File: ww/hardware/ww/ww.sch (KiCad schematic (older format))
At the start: 20 parts

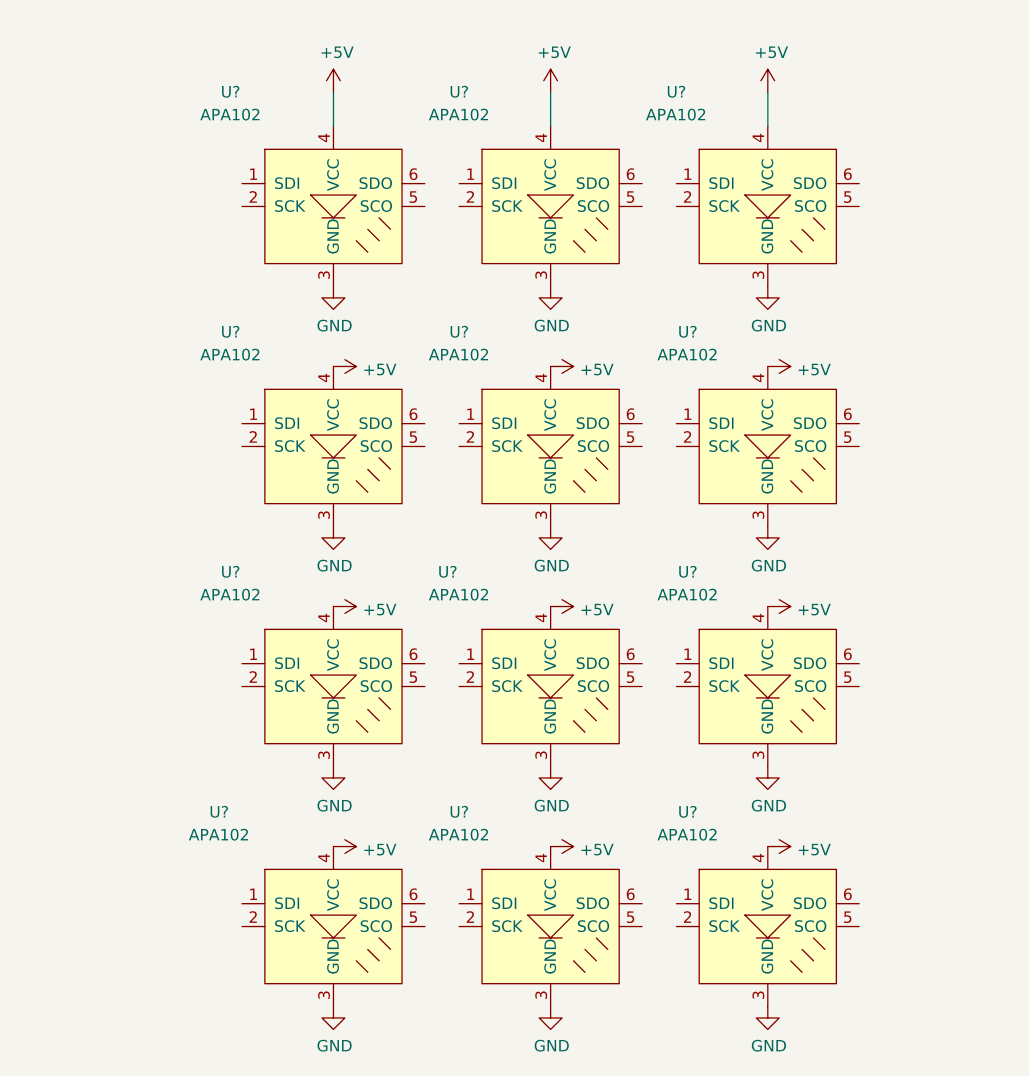
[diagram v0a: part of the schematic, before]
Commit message: Connect APA lights together
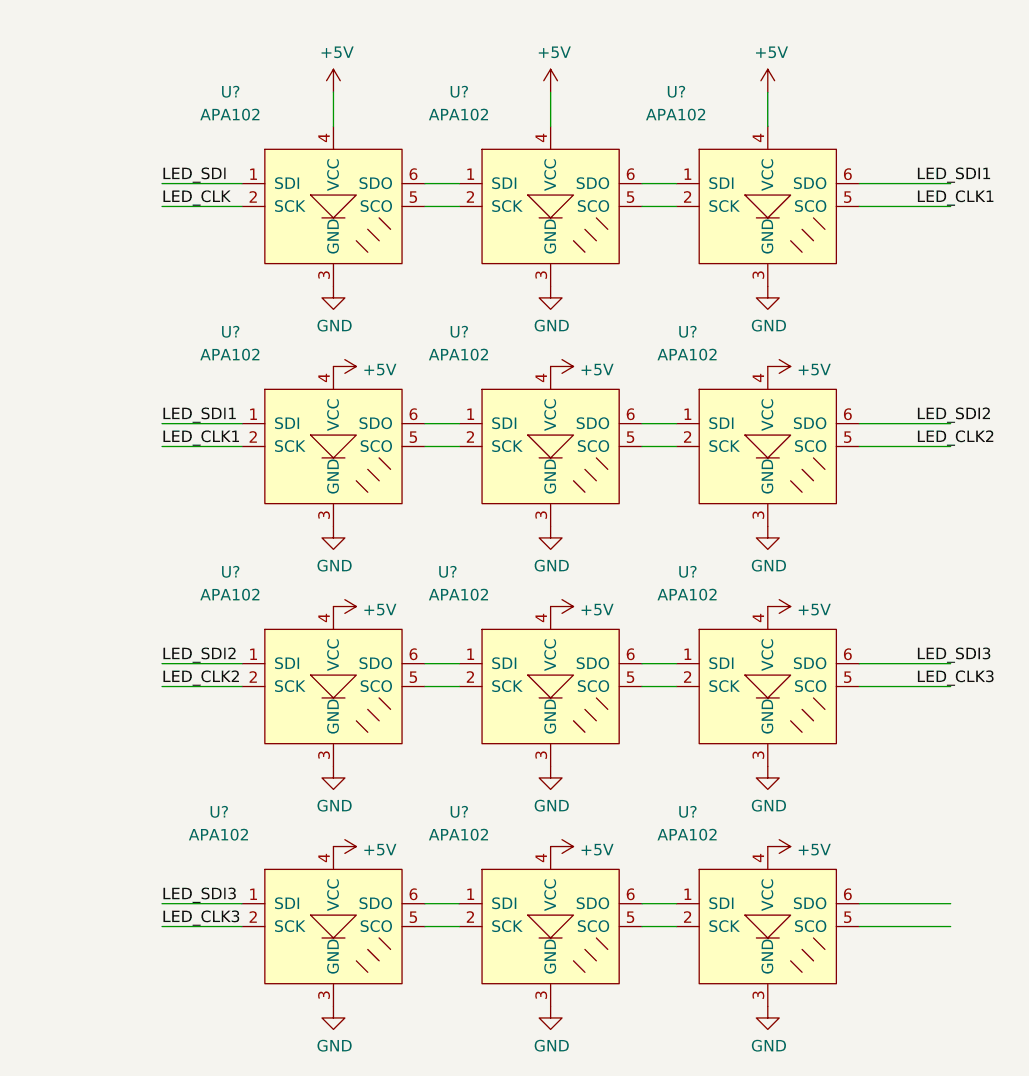
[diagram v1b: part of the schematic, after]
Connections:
- net labels added: LED_CLK, LED_CLK1, LED_CLK2, LED_CLK3, LED_SDI, LED_SDI1, LED_SDI2, LED_SDI3
- wire segments 36 -> 68
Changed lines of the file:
@@
 	1    0    0    -1
 $EndComp
+Wire Wire Line
+	8650 2350 8800 2350
+Wire Wire Line
+	8650 2450 8800 2450
+Wire Wire Line
+	9600 2350 9750 2350
+Wire Wire Line
+	9600 2450 9750 2450
+Wire Wire Line
+	8650 3400 8800 3400
+Wire Wire Line
+	8650 3500 8800 3500
+Wire Wire Line
+	9600 3400 9750 3400
+Wire Wire Line
+	9600 3500 9750 3500
+Wire Wire Line
+	8650 4450 8800 4450
+Wire Wire Line
+	8650 4550 8800 4550
+Wire Wire Line
+	9600 4450 9750 4450
+Wire Wire Line
+	9600 4550 9750 4550
+Wire Wire Line
+	8650 5500 8800 5500
+Wire Wire Line
+	8650 5600 8800 5600
+Wire Wire Line
+	9600 5500 9750 5500
+Wire Wire Line
+	9600 5600 9750 5600
+Wire Wire Line
+	7850 2350 7500 2350
+Text Label 7500 2350 0    50   ~ 0
+LED_SDI
+Wire Wire Line
+	7850 2450 7500 2450
+Text Label 7500 2450 0    50   ~ 0
+LED_CLK
+Wire Wire Line
+	7850 3400 7500 3400
+Wire Wire Line
+	7850 3500 7500 3500
+Wire Wire Line
+	7850 4450 7500 4450
+Wire Wire Line
+	7850 4550 7500 4550
+Wire Wire Line
+	7850 5500 7500 5500
+Wire Wire Line
+	7850 5600 7500 5600
+Text Label 7500 3400 0    50   ~ 0
+LED_SDI1
+Text Label 7500 3500 0    50   ~ 0
+LED_CLK1
+Text Label 7500 4450 0    50   ~ 0
+LED_SDI2
+Text Label 7500 4550 0    50   ~ 0
+LED_CLK2
+Text Label 7500 5500 0    50   ~ 0
+LED_SDI3
+Text Label 7500 5600 0    50   ~ 0
+LED_CLK3
+Wire Wire Line
+	10550 2350 10950 2350
+Wire Wire Line
+	10550 2450 10950 2450
+Wire Wire Line
+	10550 3400 10950 3400
+Wire Wire Line
+	10550 3500 10950 3500
+Wire Wire Line
+	10550 4450 10950 4450
+Wire Wire Line
+	10550 4550 10950 4550
+Wire Wire Line
+	10550 5500 10950 5500
+Wire Wire Line
+	10550 5600 10950 5600
+Text Label 10800 2350 0    50   ~ 0
+LED_SDI1
+Text Label 10800 2450 0    50   ~ 0
+LED_CLK1
+Text Label 10800 3400 0    50   ~ 0
+LED_SDI2
+Text Label 10800 3500 0    50   ~ 0
+LED_CLK2
+Text Label 10800 4450 0    50   ~ 0
+LED_SDI3
+Text Label 10800 4550 0    50   ~ 0
+LED_CLK3
 $EndSCHEMATC

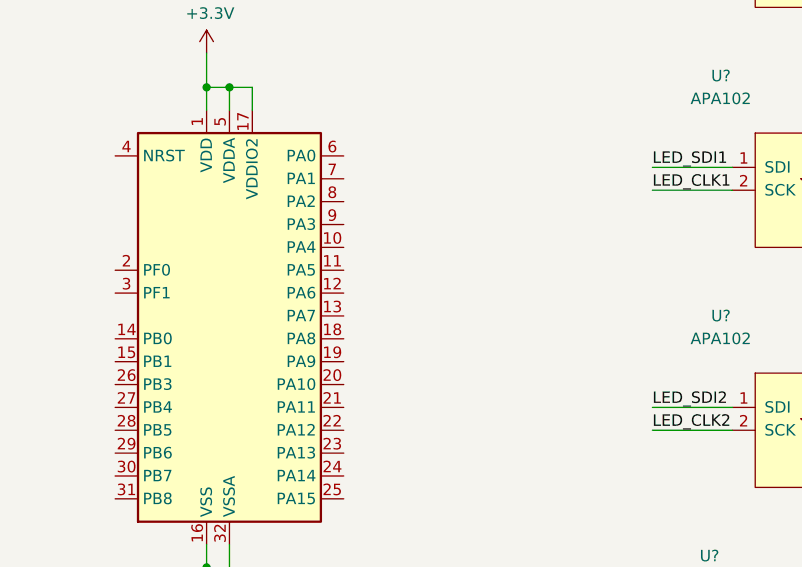
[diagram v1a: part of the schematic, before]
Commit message: Add SPI pins for controlling the LEDs
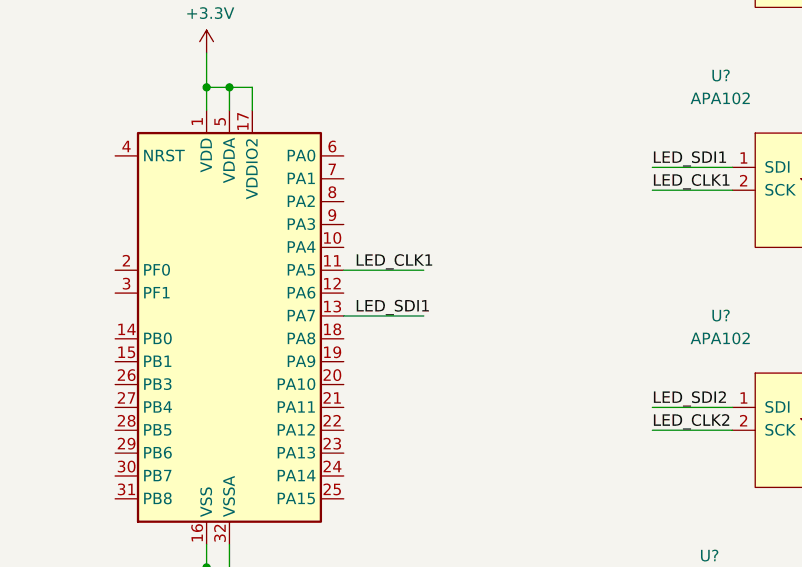
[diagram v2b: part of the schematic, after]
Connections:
- wire segments 68 -> 70
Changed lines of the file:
@@
 Text Label 10800 4550 0    50   ~ 0
 LED_CLK3
+Wire Wire Line
+	6150 3850 6500 3850
+Text Label 6200 3850 0    50   ~ 0
+LED_CLK1
+Wire Wire Line
+	6150 4050 6500 4050
+Text Label 6200 4050 0    50   ~ 0
+LED_SDI1
 $EndSCHEMATC

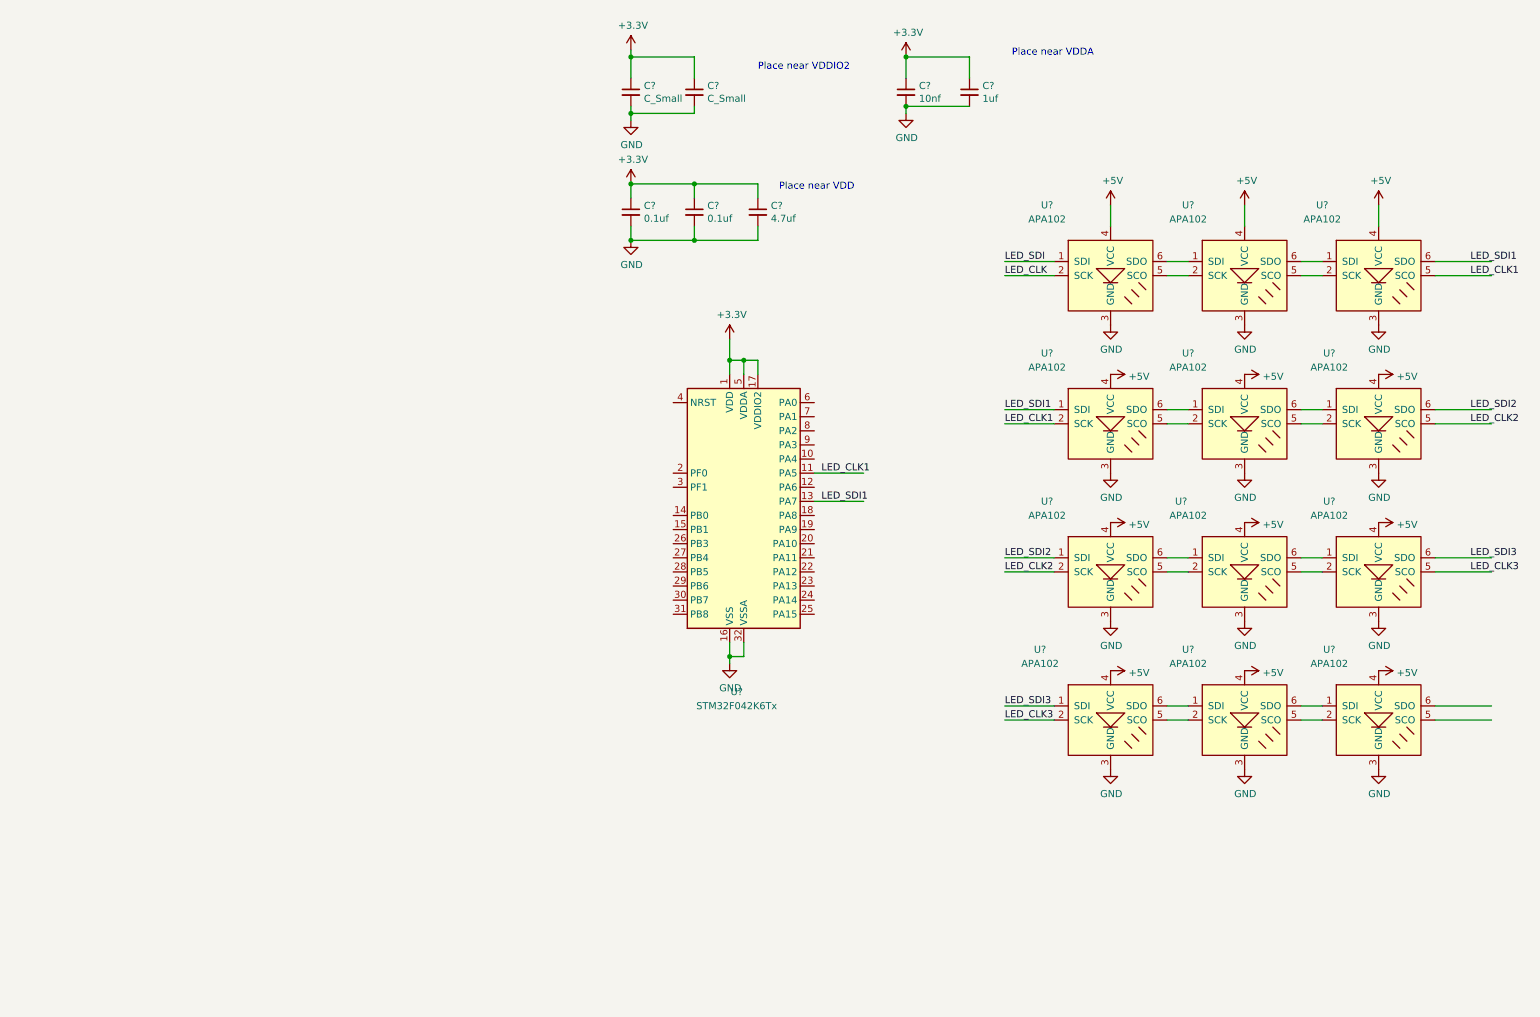
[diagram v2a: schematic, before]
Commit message: Add battery and charging system
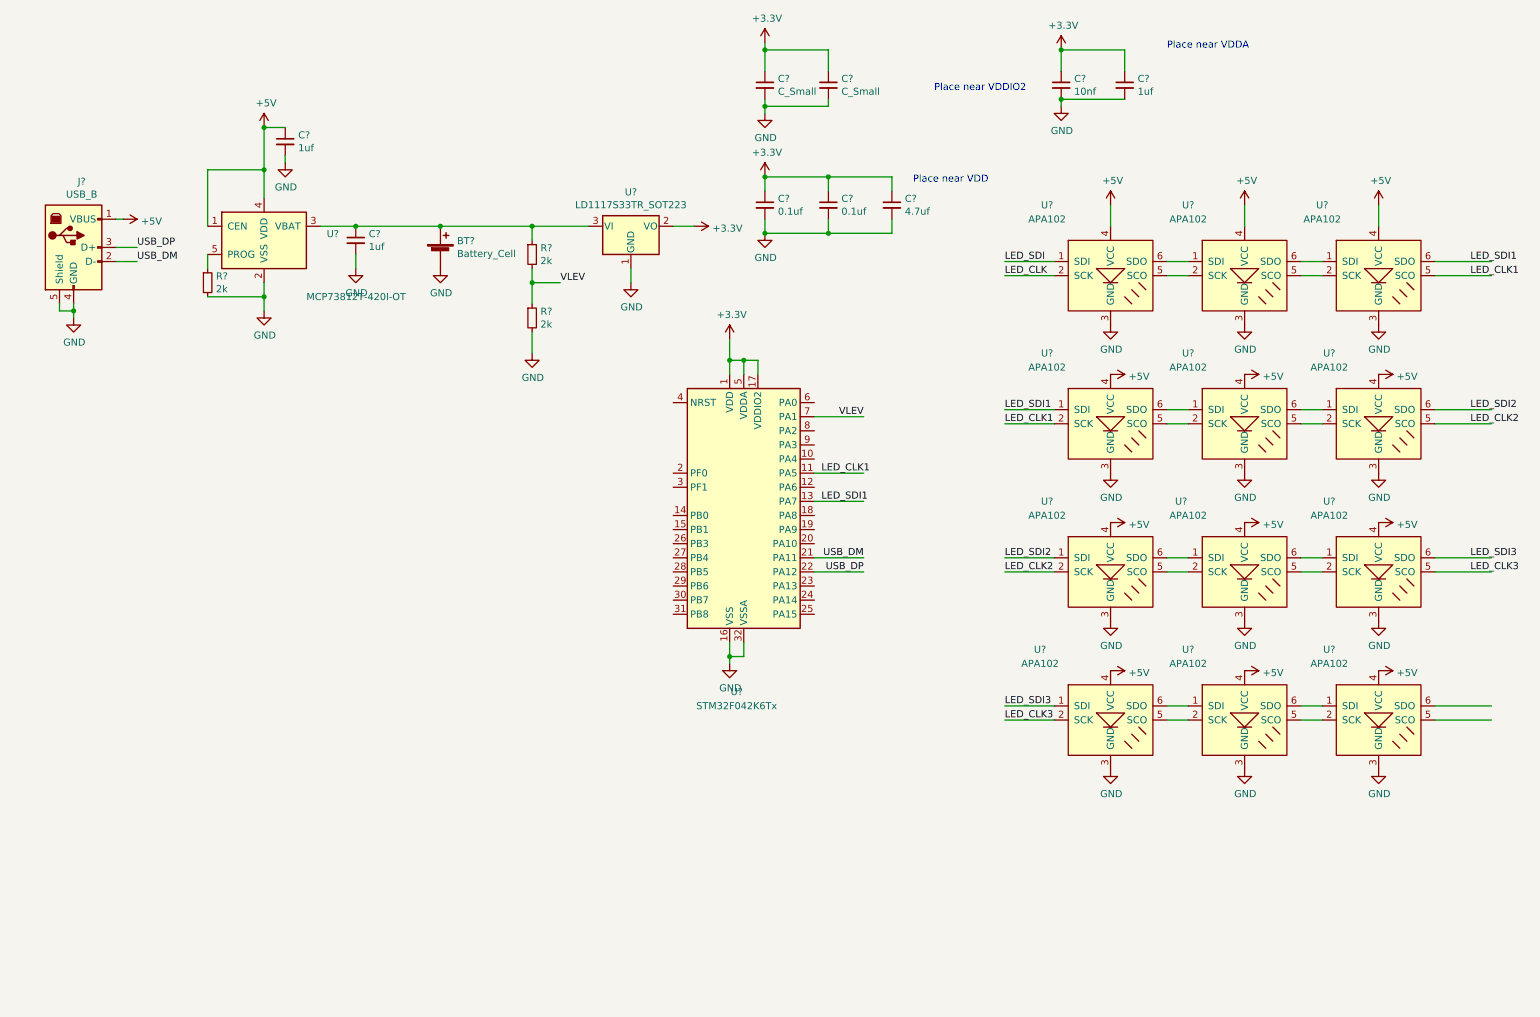
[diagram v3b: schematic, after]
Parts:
- added BT?: Battery_Cell, symbol Device:Battery_Cell
- added C? (x2): 1uf, symbol Device:C_Small
- added J?: USB_B, symbol Connector:USB_B
- added R? (x3): 2k, symbol Device:R_Small
- added U?: MCP73812T-420I-OT, Package_TO_SOT_SMD:SOT-23-5, symbol Battery_Management:MCP73812T-420I-OT
- added U?: LD1117S33TR_SOT223, Package_TO_SOT_SMD:SOT-223-3_TabPin2, symbol Regulator_Linear:LD1117S33TR_SOT223
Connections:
- net labels added: USB_DM, USB_DP, VLEV
- wire segments 70 -> 102
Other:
- moved on the sheet: C?

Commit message: Add in RTC and more power management
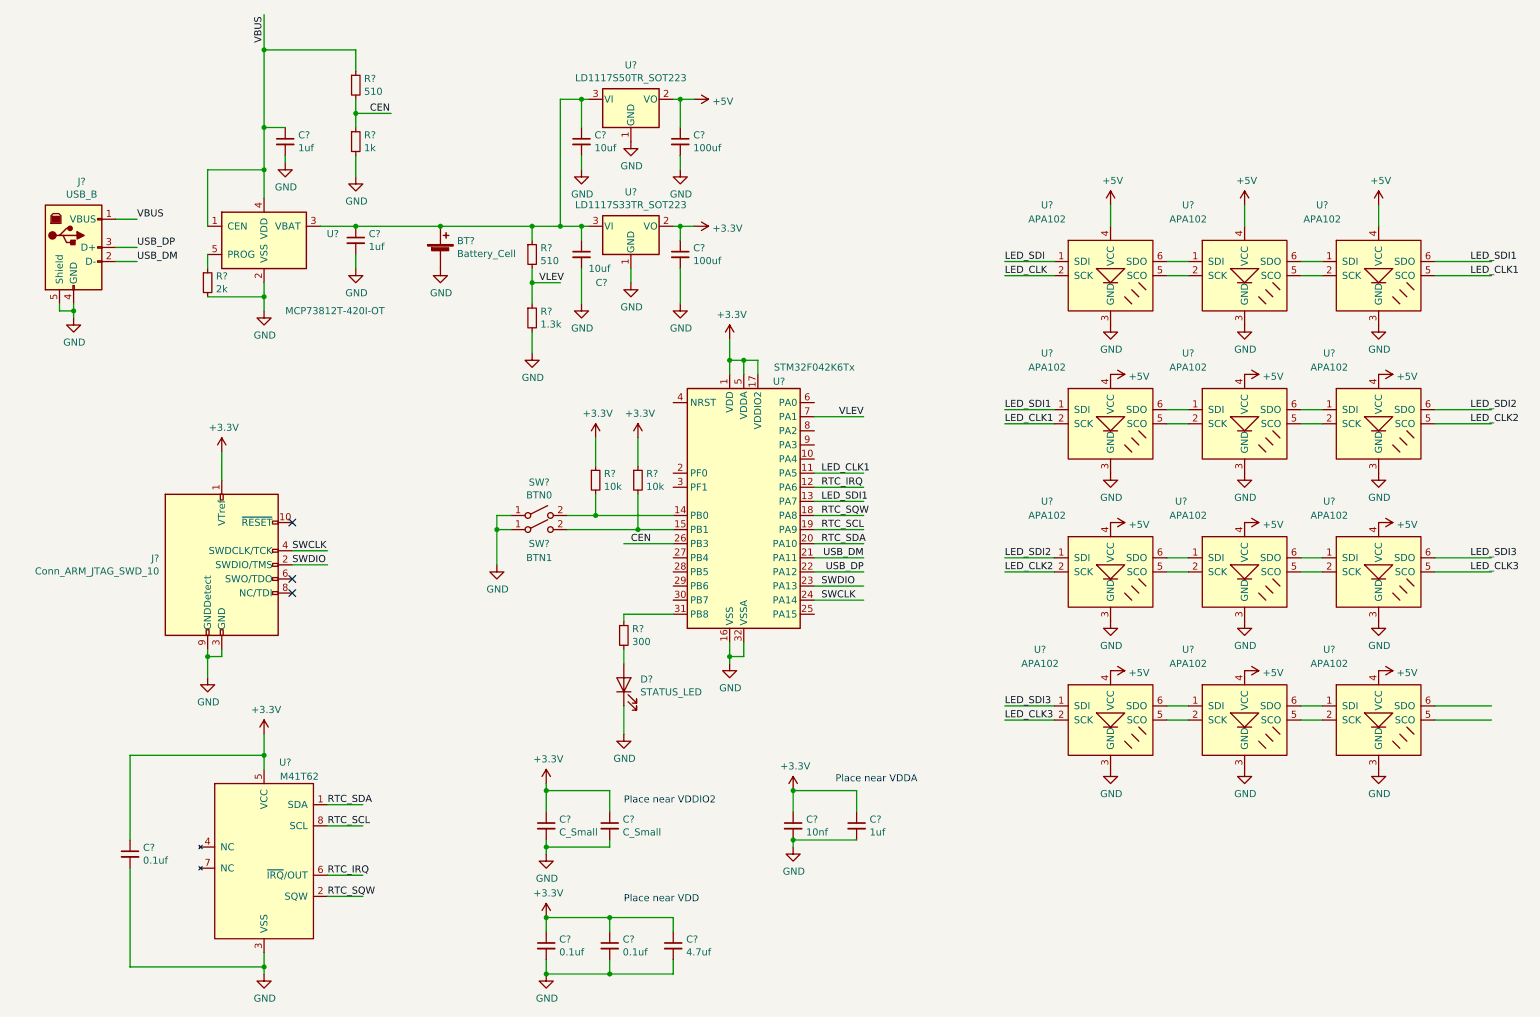
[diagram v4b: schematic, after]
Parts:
- added C? (x2): 10uf, symbol Device:C_Small
- added C? (x2): 100uf, symbol Device:C_Small
- added C?: 0.1uf, symbol Device:C_Small
- added D?: STATUS_LED, symbol Device:LED
- added J?: Conn_ARM_JTAG_SWD_10, symbol Connector:Conn_ARM_JTAG_SWD_10
- added R?: 300, symbol Device:R_Small
- added R? (x2): 10k, symbol Device:R_Small
- added R?: 510, symbol Device:R_Small
- added R?: 1k, symbol Device:R_Small
- added SW?: BTN0, symbol Switch:SW_SPST
- added SW?: BTN1, symbol Switch:SW_SPST
- added U?: LD1117S50TR_SOT223, Package_TO_SOT_SMD:SOT-223-3_TabPin2, symbol Regulator_Linear:LD1117S50TR_SOT223
- added U?: M41T62, symbol custom_ic:M41T62
- R?: value 2k -> 510
- R?: value 2k -> 1.3k
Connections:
- net labels added: CEN, RTC_IRQ, RTC_SCL, RTC_SDA, RTC_SQW, SWCLK, SWDIO, VBUS
- wire segments 102 -> 168
- no-connect marks 0 -> 3
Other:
- moved on the sheet: C?
